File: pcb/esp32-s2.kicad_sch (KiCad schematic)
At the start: 24 parts, among them J2 UART, U3 ESP32-S2FH4, Y1 X322540MPB4SI

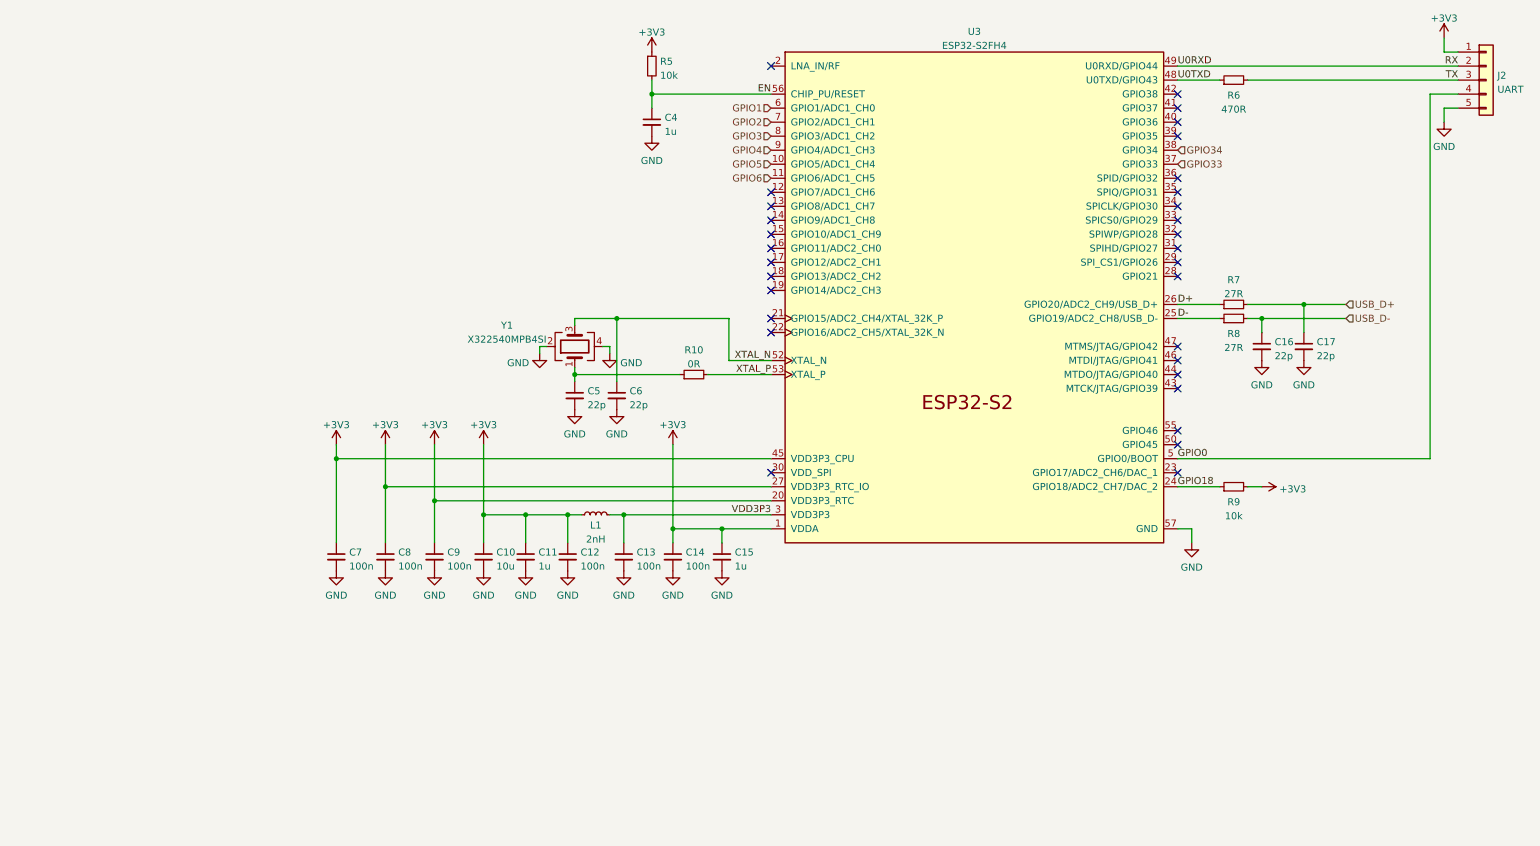
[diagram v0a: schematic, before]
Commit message: fix: add PWR_FLAGs
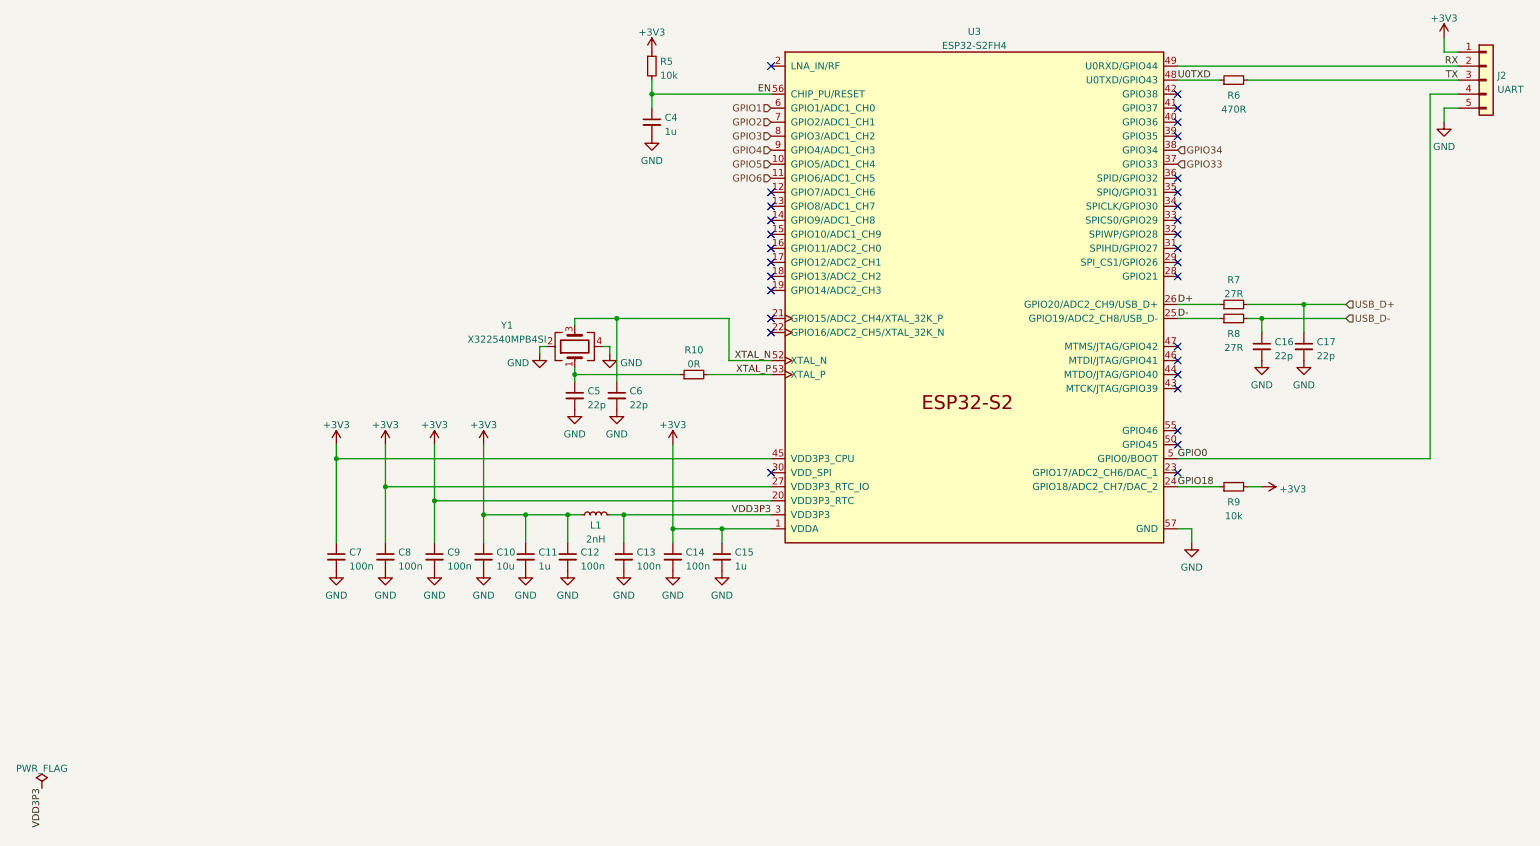
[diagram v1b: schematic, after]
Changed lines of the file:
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@@
     (effects (font (size 1.27 1.27)) (justify left bottom))
   )
-  (label "U0RXD" (at 182.88 44.45 0)
-    (effects (font (size 1.27 1.27)) (justify left bottom))
-  )
   (label "VDD3P3" (at 109.22 125.73 180)
+    (effects (font (size 1.27 1.27)) (justify right bottom))
+  )
+  (label "VDD3P3" (at -22.86 175.26 270)
     (effects (font (size 1.27 1.27)) (justify right bottom))
   )
@@
       (effects (font (size 1.27 1.27)) hide)
     )
+    (pin "1")
+  )
+  (symbol (lib_id "power:PWR_FLAG") (at -22.86 175.26 0) (unit 1)
+    (in_bom yes) (on_board yes) (fields_autoplaced)
+    (property "Reference" "#FLG?" (id 0) (at -22.86 173.355 0)
+      (effects (font (size 1.27 1.27)) hide)
+    )
+    (property "Value" "PWR_FLAG" (id 1) (at -22.86 171.6842 0))
+    (property "Footprint" "" (id 2) (at -22.86 175.26 0)
+      (effects (font (size 1.27 1.27)) hide)
+    )
+    (property "Datasheet" "~" (id 3) (at -22.86 175.26 0)
+      (effects (font (size 1.27 1.27)) hide)
+    )
